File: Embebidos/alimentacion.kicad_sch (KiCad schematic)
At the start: 19 parts, among them J2 Conn_01x02_Male, U3 SPX3819M5-L-3-3, U4 MIC29302WT, U5 MIC5219-3.3YM5

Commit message: correccion lul
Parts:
- added JP?: Jumper_2_Open, symbol Jumper:Jumper_2_Open
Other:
- note added: "Jumper debe ser de de 2.54mm de separacion y 0.65mm el grosor"
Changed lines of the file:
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@@
+    (stroke (width 0) (type default) (color 0 0 0 0))
+  )
+  (polyline (pts (xy 199.39 33.02) (xy 171.45 33.02))
     (stroke (width 0) (type default) (color 0 0 0 0))
   )
@@
     (stroke (width 0) (type default) (color 0 0 0 0))
   )
+  (polyline (pts (xy 171.45 21.59) (xy 171.45 33.02))
+    (stroke (width 0) (type default) (color 0 0 0 0))
+  )
   (wire (pts (xy 57.15 77.47) (xy 57.15 80.01))
     (stroke (width 0) (type default) (color 0 0 0 0))
@@
     (stroke (width 0) (type default) (color 0 0 0 0))
   )
+  (polyline (pts (xy 199.39 21.59) (xy 199.39 33.02))
+    (stroke (width 0) (type default) (color 0 0 0 0))
+  )
   (wire (pts (xy 114.3 149.86) (xy 106.045 149.86))
     (stroke (width 0) (type default) (color 0 0 0 0))
@@
   )
   (wire (pts (xy 52.705 139.7) (xy 52.705 139.065))
+    (stroke (width 0) (type default) (color 0 0 0 0))
+  )
+  (polyline (pts (xy 171.45 21.59) (xy 199.39 21.59))
     (stroke (width 0) (type default) (color 0 0 0 0))
   )
@@
     (at 27.94 105.41 0)
     (effects (font (size 1.27 1.27)) (justify left bottom))
+  )
+  (text "Jumper debe ser de de 2.54mm de separacion\n y 0.65mm el grosor"
+    (at 200.66 38.1 0)
+    (effects (font (size 1.27 1.27) (thickness 0.254) bold italic) (justify right bottom))
   )
   (global_label "3.3Vop2" (shape input) (at 195.58 73.66 90) (fields_autoplaced)
@@
     (pin "5")
   )
+  (symbol (lib_id "Jumper:Jumper_2_Open") (at 215.9 29.21 0) (unit 1)
+    (in_bom yes) (on_board yes) (fields_autoplaced)
+    (property "Reference" "JP?" (id 0) (at 215.9 22.86 0))
+    (property "Value" "Jumper_2_Open" (id 1) (at 215.9 25.4 0))
+    (property "Footprint" "" (id 2) (at 215.9 29.21 0)
+      (effects (font (size 1.27 1.27)) hide)
+    )
+    (property "Datasheet" "~" (id 3) (at 215.9 29.21 0)
+      (effects (font (size 1.27 1.27)) hide)
+    )
+    (pin "1")
+    (pin "2")
+  )
   (symbol (lib_id "power:+5V") (at 135.89 73.66 0) (unit 1)

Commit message: wii
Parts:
- removed U3: SPX3819M5-L-3-3, Package_TO_SOT_SMD:SOT-23-5, symbol Regulator_Linear:SPX3819M5-L-3-3
- removed U5: MIC5219-3.3YM5, Package_TO_SOT_SMD:SOT-23-5, symbol Regulator_Linear:MIC5219-3.3YM5
- added Q32: DMP3056LSDQ-13, DMP3056LSD:SOIC127P600X175-8N, symbol DMP3056LSDQ-13:DMP3056LSDQ-13
- added U?: MIC5219-3.3YM5, Package_TO_SOT_SMD:SOT-23-5, symbol Regulator_Linear:MIC5219-3.3YM5
- added U?: SPX3819M5-L-3-3, Package_TO_SOT_SMD:SOT-23-5, symbol Regulator_Linear:SPX3819M5-L-3-3
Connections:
- net +3.3V: now also U?.5 (OUT)
- net +5V: now also U?.1 (IN), U?.1 (IN)
- net 3.3Vop2: now also U?.5 (OUT)
- net CtrlOnOff: now also U?.3 (EN), U?.3 (EN)
- net GND: now also U?.2 (GND), U?.2 (GND)
- net at C10.1: now also U?.4 (BP)
- new net: Q32.7, Q32.8
- new net: Q32.5, Q32.6

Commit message: transistores traseros
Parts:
- removed Q32: DMP3056LSDQ-13, DMP3056LSD:SOIC127P600X175-8N, symbol DMP3056LSDQ-13:DMP3056LSDQ-13

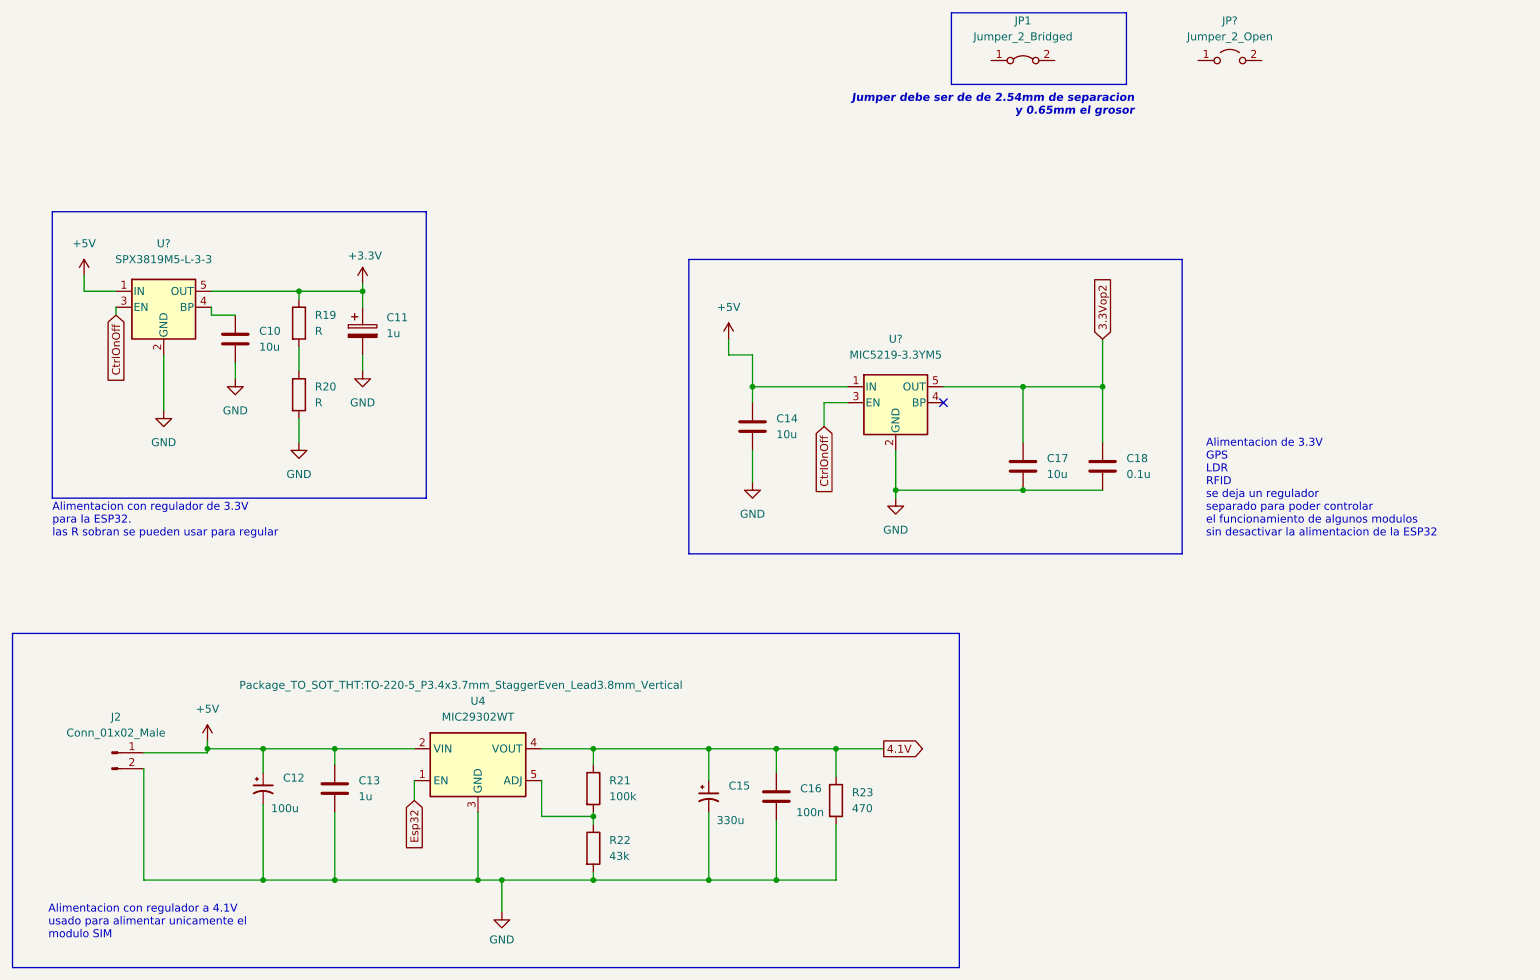
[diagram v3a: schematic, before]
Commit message: Cambio de anotacion y Vcc ldr
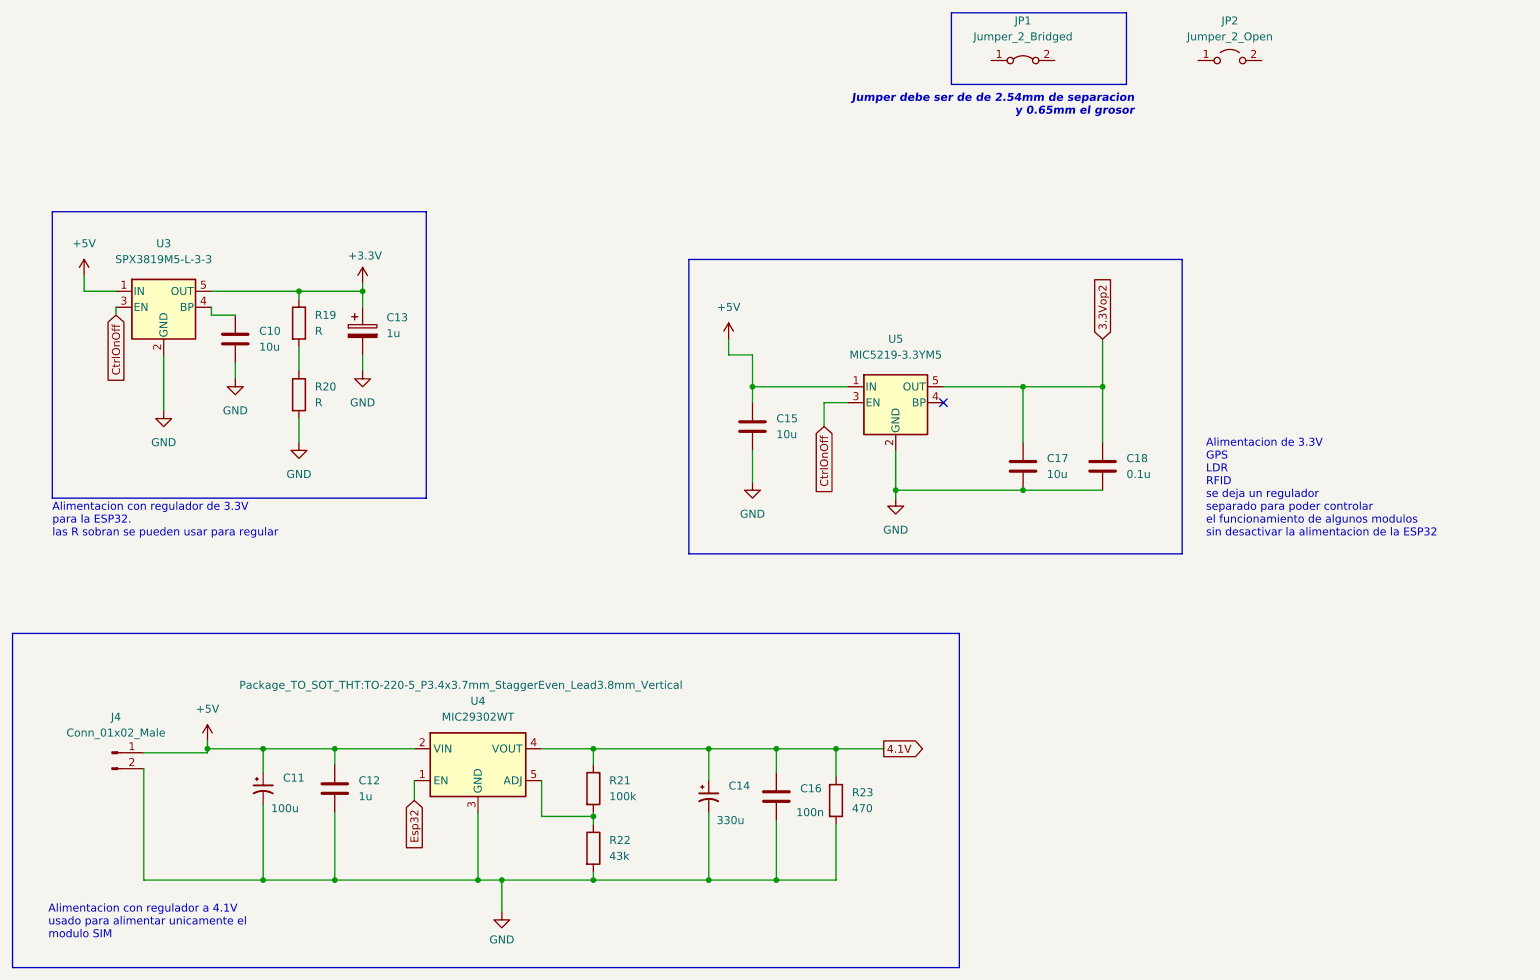
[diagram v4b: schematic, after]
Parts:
- gave numbers to parts that had none: 3
- renumbered C12 to C11, C13 to C12, C11 to C13, C15 to C14, C14 to C15, J2 to J4
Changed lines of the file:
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@@
   (symbol (lib_id "Device:C") (at 139.7 87.63 0) (unit 1)
     (in_bom yes) (on_board yes) (fields_autoplaced)
-    (property "Reference" "C14" (id 0) (at 143.51 86.3599 0)
+    (property "Reference" "C15" (id 0) (at 143.51 86.3599 0)
       (effects (font (size 1.27 1.27)) (justify left))
     )
@@
   (symbol (lib_id "power:GND") (at 67.31 90.17 0) (unit 1)
     (in_bom yes) (on_board yes) (fields_autoplaced)
-    (property "Reference" "#PWR026" (id 0) (at 67.31 96.52 0)
+    (property "Reference" "#PWR028" (id 0) (at 67.31 96.52 0)
       (effects (font (size 1.27 1.27)) hide)
     )
@@
   (symbol (lib_id "power:GND") (at 139.7 96.52 0) (unit 1)
     (in_bom yes) (on_board yes) (fields_autoplaced)
-    (property "Reference" "#PWR032" (id 0) (at 139.7 102.87 0)
+    (property "Reference" "#PWR033" (id 0) (at 139.7 102.87 0)
       (effects (font (size 1.27 1.27)) hide)
     )
@@
   (symbol (lib_id "power:GND") (at 57.15 80.01 0) (unit 1)
     (in_bom yes) (on_board yes) (fields_autoplaced)
-    (property "Reference" "#PWR025" (id 0) (at 57.15 86.36 0)
+    (property "Reference" "#PWR027" (id 0) (at 57.15 86.36 0)
       (effects (font (size 1.27 1.27)) hide)
     )
@@
   (symbol (lib_id "power:GND") (at 162.56 99.06 0) (unit 1)
     (in_bom yes) (on_board yes) (fields_autoplaced)
-    (property "Reference" "#PWR033" (id 0) (at 162.56 105.41 0)
+    (property "Reference" "#PWR034" (id 0) (at 162.56 105.41 0)
       (effects (font (size 1.27 1.27)) hide)
     )
@@
   (symbol (lib_id "Device:C") (at 73.025 145.415 0) (unit 1)
     (in_bom yes) (on_board yes) (fields_autoplaced)
-    (property "Reference" "C13" (id 0) (at 76.835 144.1449 0)
+    (property "Reference" "C12" (id 0) (at 76.835 144.1449 0)
       (effects (font (size 1.27 1.27)) (justify left))
     )
@@
   (symbol (lib_id "Regulator_Linear:MIC5219-3.3YM5") (at 162.56 83.82 0) (unit 1)
     (in_bom yes) (on_board yes) (fields_autoplaced)
-    (property "Reference" "U?" (id 0) (at 162.56 73.66 0))
+    (property "Reference" "U5" (id 0) (at 162.56 73.66 0))
     (property "Value" "MIC5219-3.3YM5" (id 1) (at 162.56 76.2 0))
     (property "Footprint" "Package_TO_SOT_SMD:SOT-23-5" (id 2) (at 162.56 75.565 0)
@@
   (symbol (lib_id "power:GND") (at 77.47 78.74 0) (unit 1)
     (in_bom yes) (on_board yes) (fields_autoplaced)
-    (property "Reference" "#PWR028" (id 0) (at 77.47 85.09 0)
+    (property "Reference" "#PWR030" (id 0) (at 77.47 85.09 0)
       (effects (font (size 1.27 1.27)) hide)
     )
@@
   (symbol (lib_id "power:+3.3V") (at 77.47 64.77 0) (unit 1)
     (in_bom yes) (on_board yes)
-    (property "Reference" "#PWR027" (id 0) (at 77.47 68.58 0)
+    (property "Reference" "#PWR029" (id 0) (at 77.47 68.58 0)
       (effects (font (size 1.27 1.27)) hide)
     )
@@
   (symbol (lib_id "power:GND") (at 45.72 85.09 0) (unit 1)
     (in_bom yes) (on_board yes) (fields_autoplaced)
-    (property "Reference" "#PWR024" (id 0) (at 45.72 91.44 0)
+    (property "Reference" "#PWR025" (id 0) (at 45.72 91.44 0)
       (effects (font (size 1.27 1.27)) hide)
     )
@@
   (symbol (lib_id "Device:C_Polarized_Small_US") (at 132.715 146.685 0) (unit 1)
     (in_bom yes) (on_board yes)
-    (property "Reference" "C15" (id 0) (at 135.89 144.9831 0)
+    (property "Reference" "C14" (id 0) (at 135.89 144.9831 0)
       (effects (font (size 1.27 1.27)) (justify left))
     )
@@
   (symbol (lib_id "Jumper:Jumper_2_Open") (at 215.9 29.21 0) (unit 1)
     (in_bom yes) (on_board yes) (fields_autoplaced)
-    (property "Reference" "JP?" (id 0) (at 215.9 22.86 0))
+    (property "Reference" "JP2" (id 0) (at 215.9 22.86 0))
     (property "Value" "Jumper_2_Open" (id 1) (at 215.9 25.4 0))
     (property "Footprint" "" (id 2) (at 215.9 29.21 0)
@@
   (symbol (lib_id "power:+5V") (at 135.89 73.66 0) (unit 1)
     (in_bom yes) (on_board yes) (fields_autoplaced)
-    (property "Reference" "#PWR030" (id 0) (at 135.89 77.47 0)
+    (property "Reference" "#PWR032" (id 0) (at 135.89 77.47 0)
       (effects (font (size 1.27 1.27)) hide)
     )
@@
   (symbol (lib_id "Regulator_Linear:SPX3819M5-L-3-3") (at 45.72 68.58 0) (unit 1)
     (in_bom yes) (on_board yes) (fields_autoplaced)
-    (property "Reference" "U?" (id 0) (at 45.72 58.42 0))
+    (property "Reference" "U3" (id 0) (at 45.72 58.42 0))
     (property "Value" "SPX3819M5-L-3-3" (id 1) (at 45.72 60.96 0))
     (property "Footprint" "Package_TO_SOT_SMD:SOT-23-5" (id 2) (at 45.72 60.325 0)
@@
   (symbol (lib_id "Device:C_Polarized_Small_US") (at 61.595 145.415 0) (unit 1)
     (in_bom yes) (on_board yes)
-    (property "Reference" "C12" (id 0) (at 64.77 143.7131 0)
+    (property "Reference" "C11" (id 0) (at 64.77 143.7131 0)
       (effects (font (size 1.27 1.27)) (justify left))
     )
@@
   (symbol (lib_id "power:+5V") (at 33.02 63.5 0) (unit 1)
     (in_bom yes) (on_board yes) (fields_autoplaced)
-    (property "Reference" "#PWR023" (id 0) (at 33.02 67.31 0)
+    (property "Reference" "#PWR024" (id 0) (at 33.02 67.31 0)
       (effects (font (size 1.27 1.27)) hide)
     )
@@
   (symbol (lib_id "Connector:Conn_01x02_Male") (at 37.465 139.7 0) (unit 1)
     (in_bom yes) (on_board yes) (fields_autoplaced)
-    (property "Reference" "J2" (id 0) (at 38.1 133.985 0))
+    (property "Reference" "J4" (id 0) (at 38.1 133.985 0))
     (property "Value" "Conn_01x02_Male" (id 1) (at 38.1 136.525 0))
     (property "Footprint" "" (id 2) (at 37.465 139.7 0)
@@
   (symbol (lib_id "Device:C_Polarized") (at 77.47 72.39 0) (unit 1)
     (in_bom yes) (on_board yes) (fields_autoplaced)
-    (property "Reference" "C11" (id 0) (at 81.28 70.2309 0)
+    (property "Reference" "C13" (id 0) (at 81.28 70.2309 0)
       (effects (font (size 1.27 1.27)) (justify left))
     )
@@
   (symbol (lib_id "power:+5V") (at 52.705 137.795 0) (unit 1)
     (in_bom yes) (on_board yes) (fields_autoplaced)
-    (property "Reference" "#PWR029" (id 0) (at 52.705 141.605 0)
-      (effects (font (size 1.27 1.27)) hide)
-    )
+    (property "Reference" "#PWR026" (id 0) (at 52.705 141.605 0)
+      (effects (font (size 1.27 1.27)) hide)
+    )
